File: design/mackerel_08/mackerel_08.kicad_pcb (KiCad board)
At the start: 2 copper layers, 13 parts, among them U1 MC68008FN, X1 CXO_DIP14

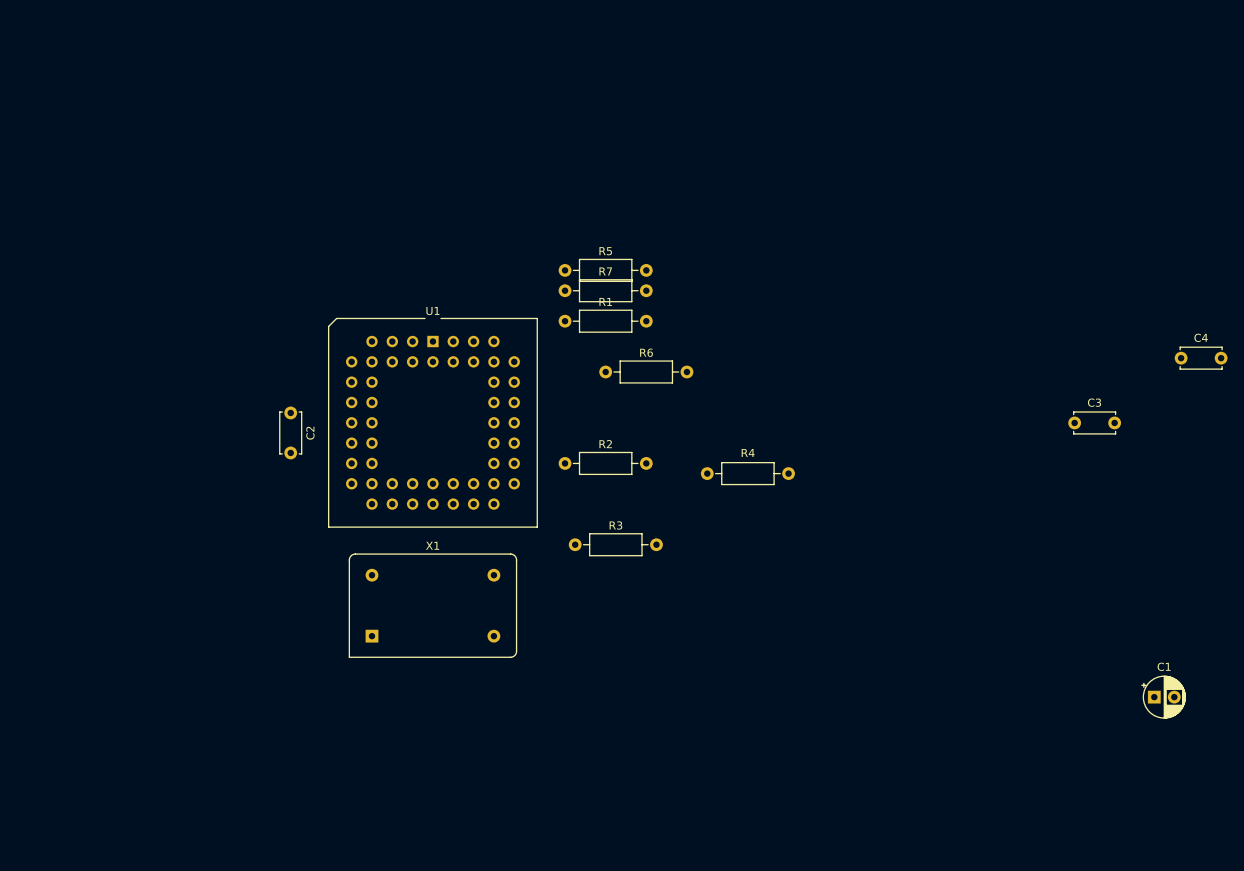
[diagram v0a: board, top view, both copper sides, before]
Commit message: CPU and decoder board schematic in progress
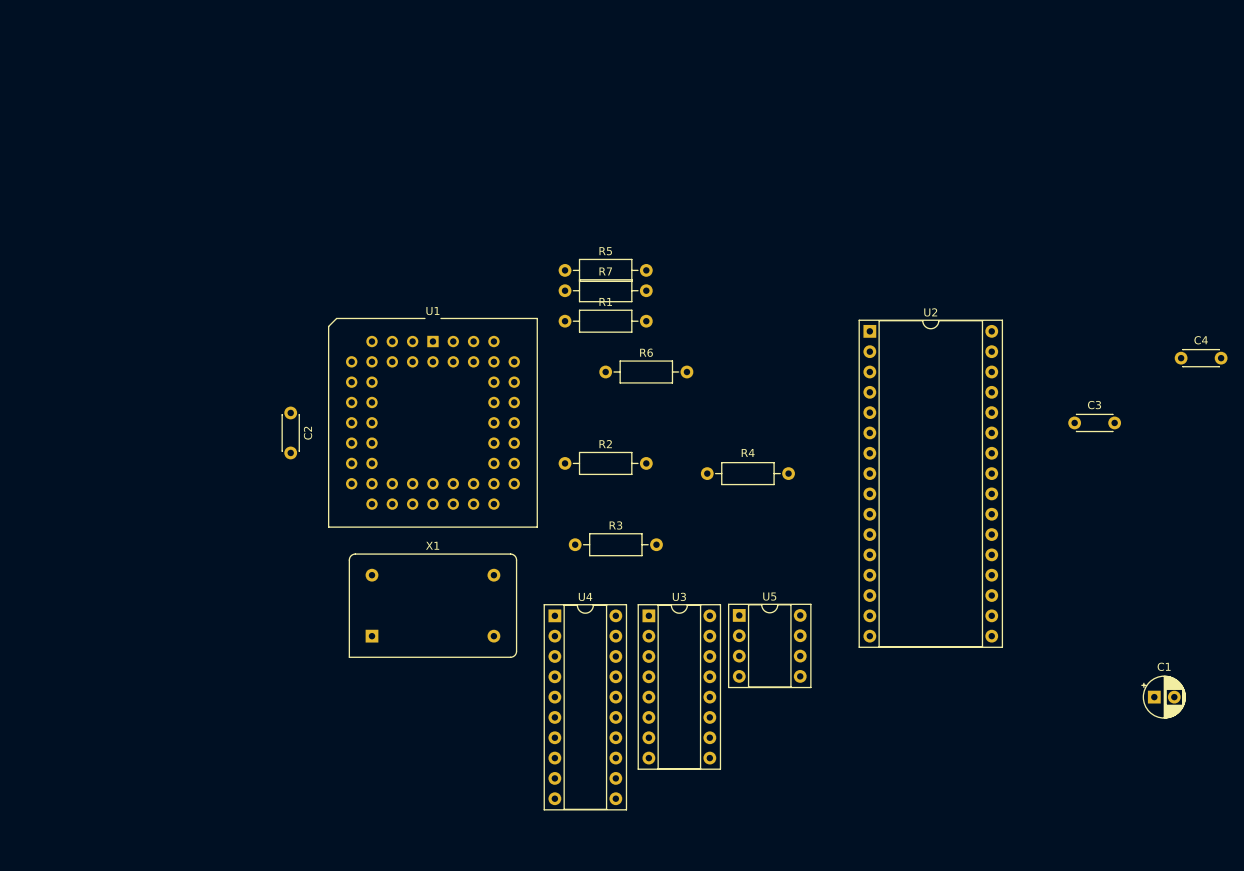
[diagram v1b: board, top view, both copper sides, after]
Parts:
- added U2: SST39SF040, Package_DIP:DIP-32_W15.24mm_Socket, F.Cu at (132.1, 64.8)
- added U3: 74HC595, Package_DIP:DIP-16_W7.62mm_Socket, F.Cu at (104.5, 100.3)
- added U4: GAL16V8, Package_DIP:DIP-20_W7.62mm_Socket, F.Cu at (92.7, 100.3)
- added U5: NE555P, Package_DIP:DIP-8_W7.62mm_Socket, F.Cu at (115.8, 100.3)
- C2, C3, C4: footprint Capacitor_THT:C_Disc_D5.0mm_W2.5mm_P5.00mm -> Capacitor_THT:C_Disc_D4.3mm_W1.9mm_P5.00mm

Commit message: Defined system bus pinout and GAL decoding schematic
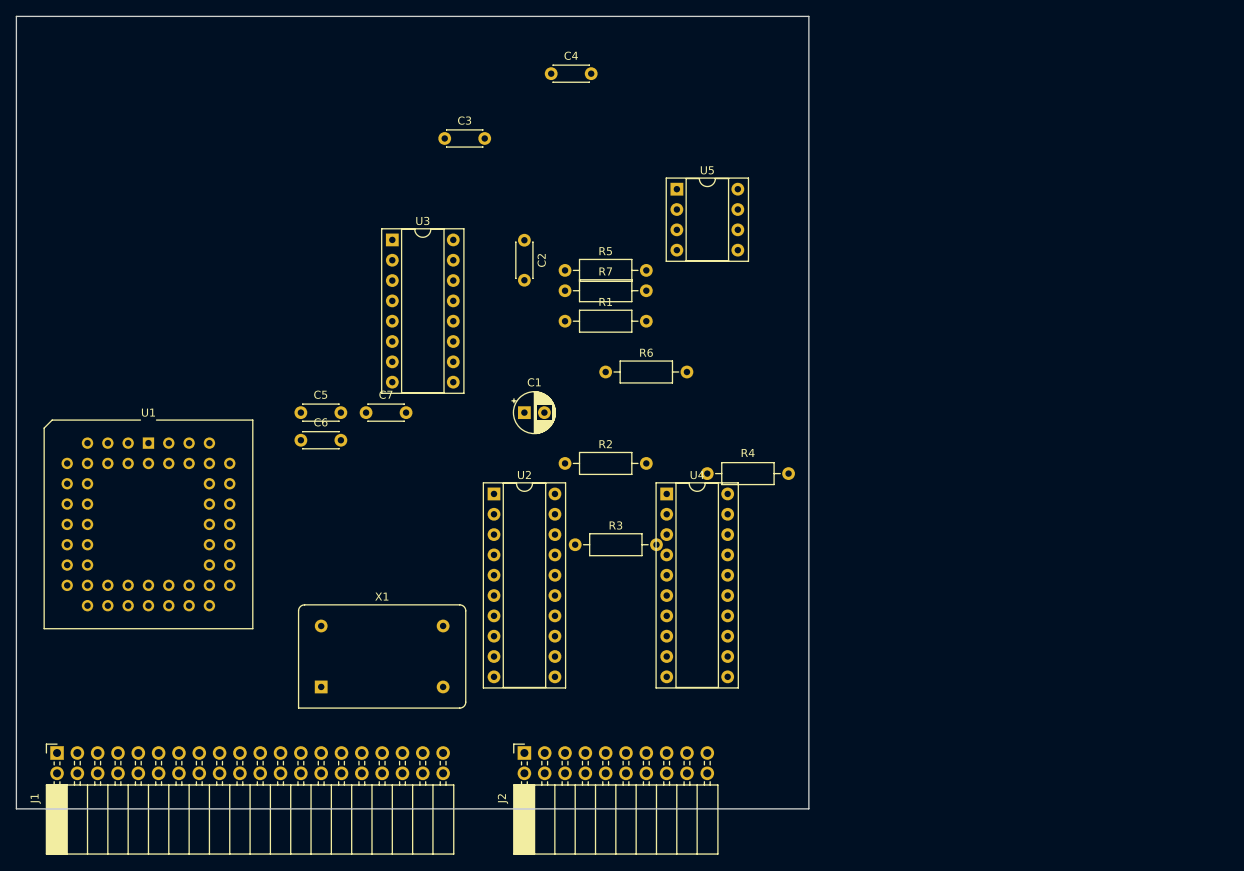
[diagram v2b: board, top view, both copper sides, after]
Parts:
- added C5: 0.1u, Capacitor_THT:C_Disc_D4.3mm_W1.9mm_P5.00mm, F.Cu at (61.0, 74.9)
- added C6: 0.1u, Capacitor_THT:C_Disc_D4.3mm_W1.9mm_P5.00mm, F.Cu at (61.0, 78.4)
- added C7: 0.1u, Capacitor_THT:C_Disc_D4.3mm_W1.9mm_P5.00mm, F.Cu at (69.1, 74.9)
- added J1: Conn_02x20_Odd_Even, Connector_PinSocket_2.54mm:PinSocket_2x20_P2.54mm_Horizontal, F.Cu at (30.5, 117.5)
- added J2: Conn_02x10_Odd_Even, Connector_PinSocket_2.54mm:PinSocket_2x10_P2.54mm_Horizontal, F.Cu at (88.9, 117.5)
- U2: value SST39SF040 -> GAL16V8; footprint Package_DIP:DIP-32_W15.24mm_Socket -> Package_DIP:DIP-20_W7.62mm_Socket
- moved C3 86.4 mm to (78.9, 40.7)
- moved C4 86.4 mm to (92.3, 32.6)
- moved C1 86.4 mm to (88.9, 74.9)
- moved U3 56.9 mm to (72.4, 53.3)
- moved U5 53.8 mm to (108.0, 47.0)
- moved U2 51.2 mm to (85.1, 85.1)
- moved U1 37.8 mm to (41.9, 78.7)
- moved C2 36.3 mm to (88.9, 53.4)
- moved U4 20.7 mm to (106.7, 85.1)
- moved X1 8.98 mm to (63.5, 109.2)
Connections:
- net Net-(U1-Pad38) renamed /CLK
- R5 pad 1: Net-(R5-Pad1) -> +5V
- R5 pad 2: +5V -> /~{IPL0}
- R6 pad 1: Net-(R6-Pad1) -> +5V
- R6 pad 2: +5V -> /~{IPL1}
- R7 pad 1: Net-(R7-Pad1) -> +5V
- R7 pad 2: +5V -> /~{IPL2}
- U1 pad 31: unconnected-(U1-Pad31) -> /~{AS}
- U1 pad 32: unconnected-(U1-Pad32) -> /~{DS}
- U1 pad 33: unconnected-(U1-Pad33) -> /RW
- U1 pad 34: unconnected-(U1-Pad34) -> /~{DTACK_CPU}
- U1 pad 45: Net-(R6-Pad1) -> /~{IPL1}
- U1 pad 46: Net-(R7-Pad1) -> /~{IPL2}
- U1 pad 47: Net-(R5-Pad1) -> /~{IPL0}
- U1 pad 48: unconnected-(U1-Pad48) -> /FC2
- U1 pad 49: unconnected-(U1-Pad49) -> /FC1
- U1 pad 50: unconnected-(U1-Pad50) -> /FC0
- U2 pad 1: /A18 -> /~{AS}
- U2 pad 10: /A2 -> GND
- U2 pad 11: /A1 -> unconnected-(U2-Pad11)
- U2 pad 12: /A0 -> /FC2
- U2 pad 13: /D0 -> /FC1
- U2 pad 14: /D1 -> /FC0
- U2 pad 15: /D2 -> /IACK
- U2 pad 16: GND -> unconnected-(U2-Pad16)
- U2 pad 17: /D3 -> /~{IPL2}
- U2 pad 18: /D4 -> /~{IPL1}
- U2 pad 19: /D5 -> /~{IPL0}
- U2 pad 2: /A16 -> /~{IRQ1}
- U2 pad 20: /D6 -> +5V
- U2 pad 3: /A15 -> /~{IRQ2}
- U2 pad 4: /A12 -> /~{IRQ3}
- U2 pad 5: /A7 -> /~{IRQ4}
- U2 pad 6: /A6 -> /~{IRQ5}
- U2 pad 7: /A5 -> /~{IRQ6}
- U2 pad 8: /A4 -> /~{IRQ7}
- U2 pad 9: /A3 -> unconnected-(U2-Pad9)
- U3 pad 10: unconnected-(U3-Pad10) -> /~{RST_OUT}
- U3 pad 11: unconnected-(U3-Pad11) -> /~{AS}
- U3 pad 12: unconnected-(U3-Pad12) -> /~{AS}
- U3 pad 13: unconnected-(U3-Pad13) -> GND
- U3 pad 14: unconnected-(U3-Pad14) -> +5V
- U3 pad 16: unconnected-(U3-Pad16) -> +5V
- U3 pad 7: unconnected-(U3-Pad7) -> /BOOT
- U3 pad 8: unconnected-(U3-Pad8) -> GND
- U4 pad 1: unconnected-(U4-Pad1) -> /BOOT
- U4 pad 10: unconnected-(U4-Pad10) -> GND
- U4 pad 11: unconnected-(U4-Pad11) -> /A21
- U4 pad 15: unconnected-(U4-Pad15) -> /~{DTACK_EXT}
- U4 pad 16: unconnected-(U4-Pad16) -> /~{DTACK_CPU}
- U4 pad 17: unconnected-(U4-Pad17) -> /~{CS_IO}
- U4 pad 18: unconnected-(U4-Pad18) -> /~{CS_RAM}
- U4 pad 19: unconnected-(U4-Pad19) -> /~{CS_ROM}
- U4 pad 2: unconnected-(U4-Pad2) -> /~{AS}
- U4 pad 20: unconnected-(U4-Pad20) -> +5V
- U4 pad 3: unconnected-(U4-Pad3) -> /IACK
- U4 pad 4: unconnected-(U4-Pad4) -> /A15
- U4 pad 5: unconnected-(U4-Pad5) -> /A16
- U4 pad 6: unconnected-(U4-Pad6) -> /A17
- U4 pad 7: unconnected-(U4-Pad7) -> /A18
- U4 pad 8: unconnected-(U4-Pad8) -> /A19
- U4 pad 9: unconnected-(U4-Pad9) -> /A20
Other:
- board outline added: 99.1 x 99.1 mm
